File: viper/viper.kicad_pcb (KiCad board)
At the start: 2 copper layers, 127 parts, among them SW1 SW_Push, SW10 SW_Push, SW11 SW_Push, SW12 SW_Push, SW13 SW_Push, SW14 SW_Push, SW14_1 SW_Push, SW15 SW_Push, SW16 SW_Push, SW17 SW_Push, SW18 SW_Push, SW19 SW_Push, SW2 SW_Push, SW20 SW_Push, SW21 SW_Push, SW22 SW_Push, SW23 SW_Push, SW24 SW_Push, SW25 SW_Push, SW26 SW_Push, SW27 SW_Push, SW28 SW_Push, SW28_1 SW_Push, SW29 SW_Push, SW3 SW_Push, SW30 SW_Push, SW31 SW_Push, SW32 SW_Push, SW33 SW_Push, SW34 SW_Push, SW35 SW_Push, SW36 SW_Push, SW37 SW_Push, SW38 SW_Push, SW39 SW_Push, SW4 SW_Push, SW40 SW_Push, SW41 SW_Push, SW41_1 SW_Push, SW42 SW_Push, SW43 SW_Push, SW43_1 SW_Push, SW44 SW_Push, SW45 SW_Push, SW46 SW_Push, SW47 SW_Push, SW48 SW_Push, SW49 SW_Push, SW5 SW_Push, SW50 SW_Push, SW51 SW_Push, SW52 SW_Push, SW53 SW_Push, SW54 SW_Push, SW55 SW_Push, SW55_1 SW_Push, SW56 SW_Push, SW57 SW_Push, SW58 SW_Push, SW59 SW_Push, SW6 SW_Push, SW60 SW_Push, SW61 SW_Push, SW7 SW_Push, SW8 SW_Push, SW9 SW_Push

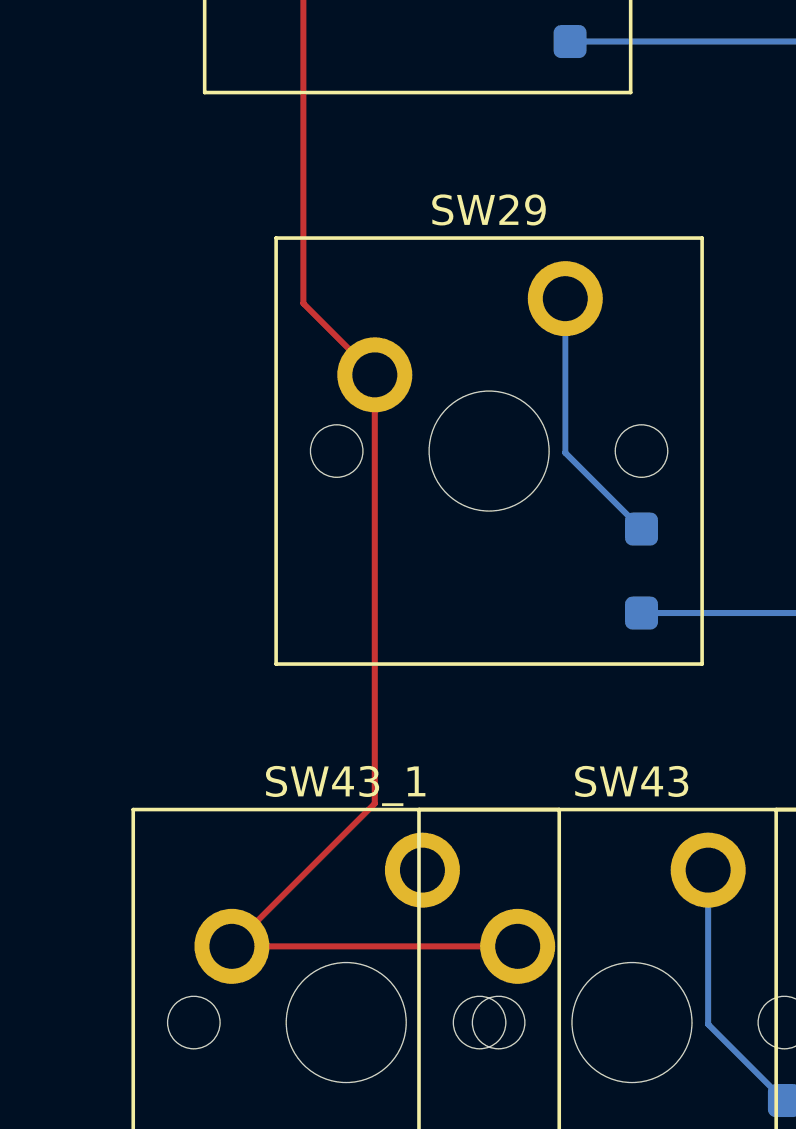
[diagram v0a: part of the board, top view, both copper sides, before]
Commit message: Add updated export with stepped caps
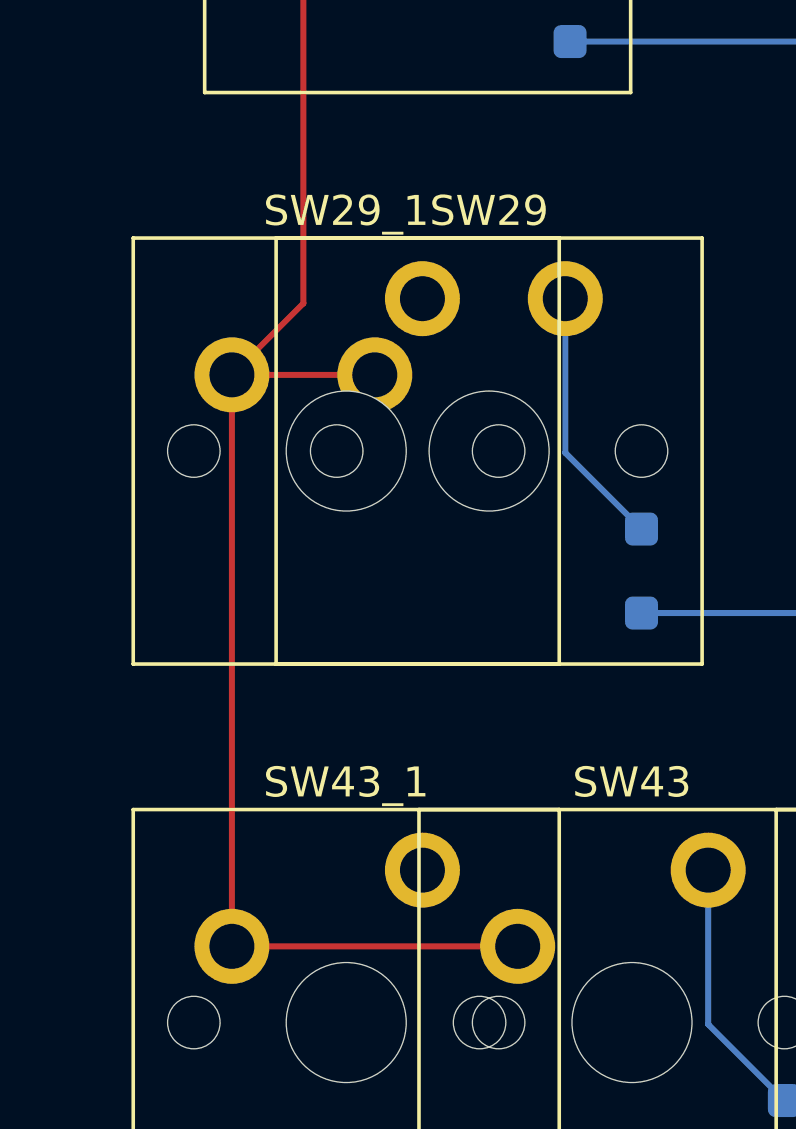
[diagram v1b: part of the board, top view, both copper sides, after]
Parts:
- added SW29_1: SW_Push, Switch_Keyboard_Cherry_MX:SW_Cherry_MX_PCB_1.00u, F.Cu at (97.6, 76.2)
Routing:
- net COL0: track 71.6 -> 74.4 mm

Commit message: kle2netlist with layout & netlist xml
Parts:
- removed SW14_1, SW28_1, SW29_1, SW41_1, SW43_1, SW55_1: SW_Push, Switch_Keyboard_Cherry_MX:SW_Cherry_MX_PCB_1.00u
- added C1: 22p, Capacitor_SMD:C_0603_1608Metric, B.Cu at (208.0, 161.7)
- added C2: 22p, Capacitor_SMD:C_0603_1608Metric, B.Cu at (207.6, 157.3)
- added C3: 0.1u, Capacitor_SMD:C_0603_1608Metric, B.Cu at (185.5, 164.3)
- added C4: 0.1u, Capacitor_SMD:C_0603_1608Metric, B.Cu at (195.3, 151.9)
- added C5: 0.1u, Capacitor_SMD:C_0603_1608Metric, B.Cu at (198.2, 169.4)
- added C6: 0.1u, Capacitor_SMD:C_0603_1608Metric, B.Cu at (185.5, 156.3)
- added C7: 4.7u, Capacitor_SMD:C_0603_1608Metric, B.Cu at (190.9, 151.9)
- added C8: 1u, Capacitor_SMD:C_0603_1608Metric, B.Cu at (195.3, 150.3)
- added D62: D, Diode_SMD:D_SOD-123F, B.Cu at (367.0, 98.3)
- added D63: D, Diode_SMD:D_SOD-123F, B.Cu at (128.9, 117.3)
- added D64: D, Diode_SMD:D_SOD-123F, B.Cu at (152.7, 117.3)
- added D65: D, Diode_SMD:D_SOD-123F, B.Cu at (233.7, 117.3)
- added D66: D, Diode_SMD:D_SOD-123F, B.Cu at (314.6, 117.3)
- added D67: D, Diode_SMD:D_SOD-123F, B.Cu at (338.5, 117.3)
- added J1: USB_C_Receptacle_USB2.0, Connector_USB:USB_C_Receptacle_XKB_U262-16XN-4BVC11, B.Cu at (192.7, 132.8)
- added R1: 22, Resistor_SMD:R_0603_1608Metric, B.Cu at (191.8, 147.8)
- added R2: 22, Resistor_SMD:R_0603_1608Metric, B.Cu at (193.5, 147.8)
- added R3: 10k, Resistor_SMD:R_0603_1608Metric, B.Cu at (190.9, 169.4)
- added R4: 10k, Resistor_SMD:R_0603_1608Metric, B.Cu at (206.0, 154.6)
- added RST: SW_SPST, Button_Switch_SMD:SW_SPST_TL3342, B.Cu at (215.7, 154.0)
- added ST14: MountingHole, PCM_Mounting_Keyboard_Stabilizer:Stabilizer_Cherry_MX_2.00u, F.Cu at (352.4, 38.1)
- added ST30: MountingHole, PCM_Mounting_Keyboard_Stabilizer:Stabilizer_Cherry_MX_2.00u, F.Cu at (359.6, 66.7)
- added ST44: MountingHole, PCM_Mounting_Keyboard_Stabilizer:Stabilizer_Cherry_MX_2.00u, F.Cu at (350.0, 76.2)
- added ST47: MountingHole, PCM_Mounting_Keyboard_Stabilizer:Stabilizer_Cherry_MX_2.00u, F.Cu at (107.2, 95.2)
- added ST60: MountingHole, PCM_Mounting_Keyboard_Stabilizer:Stabilizer_Cherry_MX_2.00u, F.Cu at (345.3, 95.2)
- added ST65: MountingHole, PCM_Mounting_Keyboard_Stabilizer:Stabilizer_Cherry_MX_7.00u, F.Cu at (228.6, 114.3)
- added SW62: SW_Push, PCM_Switch_Keyboard_Cherry_MX:SW_Cherry_MX_PCB_1.00u, F.Cu at (361.9, 95.2)
- added SW63: SW_Push, PCM_Switch_Keyboard_Cherry_MX:SW_Cherry_MX_PCB_1.00u, F.Cu at (123.8, 114.3)
- added SW64: SW_Push, PCM_Switch_Keyboard_Cherry_MX:SW_Cherry_MX_PCB_1.50u, F.Cu at (147.6, 114.3)
- added SW65: SW_Push, PCM_Switch_Keyboard_Cherry_MX:SW_Cherry_MX_PCB_7.00u, F.Cu at (228.6, 114.3)
- added SW66: SW_Push, PCM_Switch_Keyboard_Cherry_MX:SW_Cherry_MX_PCB_1.50u, F.Cu at (309.6, 114.3)
- added SW67: SW_Push, PCM_Switch_Keyboard_Cherry_MX:SW_Cherry_MX_PCB_1.00u, F.Cu at (333.4, 114.3)
- added U1: ATmega32U4-A, Package_QFP:TQFP-44_10x10mm_P0.8mm, B.Cu at (194.9, 160.3)
- added U2: TPD2S017, Package_TO_SOT_SMD:SOT-23-6, B.Cu at (192.7, 141.7)
- added Y1: Crystal_GND24, Crystal:Crystal_SMD_3225-4Pin_3.2x2.5mm, B.Cu at (205.6, 159.4)
- SW1, SW10, SW11, SW12, SW13, SW15, SW17, SW18, SW19, SW2, SW20, SW21, SW22, SW23, SW24, SW25, SW26, SW27, SW28, SW3, SW30, SW33, SW34, SW35, SW36, SW37, SW38, SW39, SW4, SW40, SW41, SW42, SW43, SW45, SW46, SW49, SW5, SW50, SW51, SW52, SW53, SW54, SW55, SW56, SW57, SW58, SW59, SW6, SW7, SW8, SW9: footprint Switch_Keyboard_Cherry_MX:SW_Cherry_MX_PCB_1.00u -> PCM_Switch_Keyboard_Cherry_MX:SW_Cherry_MX_PCB_1.00u
- SW14: footprint Switch_Keyboard_Cherry_MX:SW_Cherry_MX_PCB_1.00u -> PCM_Switch_Keyboard_Cherry_MX:SW_Cherry_MX_PCB_2.00u
- SW16, SW29: footprint Switch_Keyboard_Cherry_MX:SW_Cherry_MX_PCB_1.00u -> PCM_Switch_Keyboard_Cherry_MX:SW_Cherry_MX_PCB_1.50u
- SW31, SW61: footprint Switch_Keyboard_Cherry_MX:SW_Cherry_MX_PCB_1.00u -> PCM_Switch_Keyboard_Cherry_MX:SW_Cherry_MX_PCB_1.75u
- SW32, SW48: footprint Switch_Keyboard_Cherry_MX:SW_Cherry_MX_PCB_1.00u -> PCM_Switch_Keyboard_Cherry_MX:SW_Cherry_MX_PCB_1.25u
- SW44, SW47: footprint Switch_Keyboard_Cherry_MX:SW_Cherry_MX_PCB_1.00u -> PCM_Switch_Keyboard_Cherry_MX:SW_Cherry_MX_PCB_2.25u
- SW60: footprint Switch_Keyboard_Cherry_MX:SW_Cherry_MX_PCB_1.00u -> PCM_Switch_Keyboard_Cherry_MX:SW_Cherry_MX_PCB_2.75u
- moved D29 255.6 mm to (362.3, 60.2)
- moved SW29 255.5 mm to (357.2, 57.1)
- moved D15 243.7 mm to (348.0, 41.1)
- moved SW15 243.6 mm to (342.9, 38.1)
- moved D44 231.8 mm to (355.1, 79.2)
- moved SW44 231.8 mm to (350.0, 76.2)
- moved D30 231.2 mm to (364.6, 69.7)
- moved SW30 231.2 mm to (359.6, 66.7)
- moved D46 212.9 mm to (367.0, 41.1)
- moved D43 212.9 mm to (324.2, 79.2)
- moved SW43 212.8 mm to (319.1, 76.2)
- moved SW46 212.6 mm to (361.9, 38.1)
- moved D45 201.0 mm to (343.2, 79.2)
- moved SW45 200.9 mm to (338.1, 76.2)
- moved D57 149.0 mm to (276.5, 98.3)
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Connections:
- D15 pad 1: ROW1 -> ROW0
- D29 pad 1: ROW2 -> ROW1
- D30 pad 1: ROW2 -> ROW1
- D43 pad 1: ROW3 -> ROW2
- D44 pad 1: ROW3 -> ROW2
- D45 pad 1: ROW3 -> ROW2
- D46 pad 1: ROW3 -> ROW2
- D57 pad 1: ROW4 -> ROW3
- D58 pad 1: ROW4 -> ROW3
- D59 pad 1: ROW4 -> ROW3
- D60 pad 1: ROW4 -> ROW3
- D61 pad 1: ROW4 -> ROW3
- SW15 pad 1: COL0 -> COL13
- SW16 pad 1: COL1 -> COL0
- SW17 pad 1: COL2 -> COL1
- SW18 pad 1: COL3 -> COL2
- SW19 pad 1: COL4 -> COL3
- SW20 pad 1: COL5 -> COL4
- SW21 pad 1: COL6 -> COL5
- SW22 pad 1: COL7 -> COL6
- SW23 pad 1: COL8 -> COL7
- SW24 pad 1: COL9 -> COL8
- SW25 pad 1: COL10 -> COL9
- SW26 pad 1: COL11 -> COL10
- SW27 pad 1: COL12 -> COL11
- SW28 pad 1: COL13 -> COL12
- SW29 pad 1: COL0 -> COL13
- SW30 pad 1: COL1 -> COL13
- SW31 pad 1: COL2 -> COL0
- SW32 pad 1: COL3 -> COL0
- SW33 pad 1: COL4 -> COL1
- SW34 pad 1: COL5 -> COL2
- SW35 pad 1: COL6 -> COL3
- SW36 pad 1: COL7 -> COL4
- SW37 pad 1: COL8 -> COL5
- SW38 pad 1: COL9 -> COL6
- SW39 pad 1: COL10 -> COL7
- SW40 pad 1: COL11 -> COL8
- SW41 pad 1: COL12 -> COL9
- SW42 pad 1: COL13 -> COL10
- SW43 pad 1: COL0 -> COL11
- SW44 pad 1: COL1 -> COL12
- SW45 pad 1: COL2 -> COL12
- SW46 pad 1: COL3 -> COL13
- SW47 pad 1: COL4 -> COL0
- SW48 pad 1: COL5 -> COL0
- SW49 pad 1: COL6 -> COL1
- SW50 pad 1: COL7 -> COL2
- SW51 pad 1: COL8 -> COL3
- SW52 pad 1: COL9 -> COL4
- SW53 pad 1: COL10 -> COL5
- SW54 pad 1: COL11 -> COL6
- SW55 pad 1: COL12 -> COL7
- SW56 pad 1: COL13 -> COL8
- SW57 pad 1: COL1 -> COL9
- SW58 pad 1: COL2 -> COL10
- SW59 pad 1: COL3 -> COL11
- SW60 pad 1: COL11 -> COL12
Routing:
- net ROW3: track 254.8 -> 528.6 mm
- net ROW0: track 257.2 -> 514.3 mm
- net ROW1: track 233.4 -> 466.7 mm
- net ROW2: track 290.7 -> 504.8 mm
- net COL2: track 90.0 -> 270.0 mm
- net COL11: track 86.1 -> 258.2 mm
- net COL9: track 67.0 -> 201.0 mm
- net COL4: track 67.0 -> 201.0 mm
- net COL8: track 67.0 -> 201.0 mm
- net COL6: track 67.0 -> 201.0 mm
- net COL5: track 67.0 -> 201.0 mm
- net COL7: track 67.0 -> 201.0 mm
- net ROW4: track 209.5 -> 338.1 mm
- net COL0: track 74.4 -> 199.4 mm
- net COL10: track 44.0 -> 132.1 mm
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
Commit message: Updated kle layout
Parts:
- removed D62, D63, D64, D65, D66, D67: D, Diode_SMD:D_SOD-123F
- removed ST30, ST44, ST47, ST60: MountingHole, PCM_Mounting_Keyboard_Stabilizer:Stabilizer_Cherry_MX_2.00u
- removed ST65: MountingHole, PCM_Mounting_Keyboard_Stabilizer:Stabilizer_Cherry_MX_7.00u
- removed SW63, SW67: SW_Push, PCM_Switch_Keyboard_Cherry_MX:SW_Cherry_MX_PCB_1.00u
- removed SW64, SW66: SW_Push, PCM_Switch_Keyboard_Cherry_MX:SW_Cherry_MX_PCB_1.50u
- removed SW65: SW_Push, PCM_Switch_Keyboard_Cherry_MX:SW_Cherry_MX_PCB_7.00u
- added ST28_1: MountingHole, PCM_Mounting_Keyboard_Stabilizer:Stabilizer_Cherry_MX_2.00u, F.Cu at (111.9, 24.8)
- added ST41: MountingHole, PCM_Mounting_Keyboard_Stabilizer:Stabilizer_Cherry_MX_2.00u, F.Cu at (81.0, 24.8)
- added ST43: MountingHole, PCM_Mounting_Keyboard_Stabilizer:Stabilizer_Cherry_MX_2.00u, F.Cu at (142.7, 24.8)
- added ST55: MountingHole, PCM_Mounting_Keyboard_Stabilizer:Stabilizer_Cherry_MX_2.00u, F.Cu at (173.6, 24.8)
- added ST59: MountingHole, PCM_Mounting_Keyboard_Stabilizer:Stabilizer_Cherry_MX_7.00u, F.Cu at (95.3, 46.6)
- added SW14_1: SW_Push, PCM_Switch_Keyboard_Cherry_MX:SW_Cherry_MX_PCB_1.00u, F.Cu at (131.2, 172.3)
- added SW28_1: SW_Push, PCM_Switch_Keyboard_Cherry_MX:SW_Cherry_MX_PCB_1.00u, F.Cu at (113.7, 67.0)
- added SW29_1: SW_Push, PCM_Switch_Keyboard_Cherry_MX:SW_Cherry_MX_PCB_1.25u, F.Cu at (131.2, 137.2)
- added SW41_1: SW_Push, PCM_Switch_Keyboard_Cherry_MX:SW_Cherry_MX_PCB_1.00u, F.Cu at (148.8, 102.1)
- added SW43_1: SW_Push, PCM_Switch_Keyboard_Cherry_MX:SW_Cherry_MX_PCB_1.25u, F.Cu at (113.7, 84.6)
- added SW55_1: SW_Push, PCM_Switch_Keyboard_Cherry_MX:SW_Cherry_MX_PCB_1.75u, F.Cu at (183.9, 102.1)
- C1, C2, C3, C4, C5, C6, C7, C8, D1, D10, D11, D12, D13, D14, D15, D16, D17, D18, D19, D2, D20, D21, D22, D23, D24, D25, D26, D27, D28, D29, D3, D30, D31, D32, D33, D34, D35, D36, D37, D38, D39, D4, D40, D41, D42, D43, D44, D45, D46, D47, D48, D49, D5, D50, D51, D52, D53, D54, D55, D56, D57, D58, D59, D6, D60, D61, D7, D8, D9, R1, R2, R3, R4, RST, U2, Y1: moved to F.Cu
- J1: value USB_C_Receptacle_USB2.0 -> USB_C_Receptacle_USB2.0_14P; footprint Connector_USB:USB_C_Receptacle_XKB_U262-16XN-4BVC11 -> Connector_USB:USB_C_Receptacle_GCT_USB4105-xx-A_16P_TopMnt_Horizontal; moved to F.Cu
- SW15, SW28, SW58: footprint PCM_Switch_Keyboard_Cherry_MX:SW_Cherry_MX_PCB_1.00u -> PCM_Switch_Keyboard_Cherry_MX:SW_Cherry_MX_PCB_1.50u
- SW16: footprint PCM_Switch_Keyboard_Cherry_MX:SW_Cherry_MX_PCB_1.50u -> PCM_Switch_Keyboard_Cherry_MX:SW_Cherry_MX_PCB_1.00u
- SW29: footprint PCM_Switch_Keyboard_Cherry_MX:SW_Cherry_MX_PCB_1.50u -> PCM_Switch_Keyboard_Cherry_MX:SW_Cherry_MX_PCB_1.75u
- SW31, SW61: footprint PCM_Switch_Keyboard_Cherry_MX:SW_Cherry_MX_PCB_1.75u -> PCM_Switch_Keyboard_Cherry_MX:SW_Cherry_MX_PCB_1.00u
- SW32, SW48: footprint PCM_Switch_Keyboard_Cherry_MX:SW_Cherry_MX_PCB_1.25u -> PCM_Switch_Keyboard_Cherry_MX:SW_Cherry_MX_PCB_1.00u
- SW41, SW43: footprint PCM_Switch_Keyboard_Cherry_MX:SW_Cherry_MX_PCB_1.00u -> PCM_Switch_Keyboard_Cherry_MX:SW_Cherry_MX_PCB_2.25u
- SW44, SW47: footprint PCM_Switch_Keyboard_Cherry_MX:SW_Cherry_MX_PCB_2.25u -> PCM_Switch_Keyboard_Cherry_MX:SW_Cherry_MX_PCB_1.00u
- SW55: footprint PCM_Switch_Keyboard_Cherry_MX:SW_Cherry_MX_PCB_1.00u -> PCM_Switch_Keyboard_Cherry_MX:SW_Cherry_MX_PCB_2.75u
- SW59: footprint PCM_Switch_Keyboard_Cherry_MX:SW_Cherry_MX_PCB_1.00u -> PCM_Switch_Keyboard_Cherry_MX:SW_Cherry_MX_PCB_7.00u
- SW60: footprint PCM_Switch_Keyboard_Cherry_MX:SW_Cherry_MX_PCB_2.75u -> PCM_Switch_Keyboard_Cherry_MX:SW_Cherry_MX_PCB_1.50u
- SW62: value SW_Push -> SW_PUSH; footprint PCM_Switch_Keyboard_Cherry_MX:SW_Cherry_MX_PCB_1.00u -> Button_Switch_SMD:SW_SPST_TL3342
- U1: value ATmega32U4-A -> ATmega32U4-M; footprint Package_QFP:TQFP-44_10x10mm_P0.8mm -> Package_DFN_QFN:QFN-44-1EP_7x7mm_P0.5mm_EP5.2x5.2mm; moved to F.Cu
- moved SW62 369.4 mm to (4.28, 3.02)
- moved SW29 313.9 mm to (43.5, 67.0)
- moved SW46 304.5 mm to (61.0, 84.6)
- moved ST14 302.6 mm to (50.1, 24.8)
- moved D11 301.3 mm to (63.5, 183.8), turned to 0 degrees
- moved SW14 285.7 mm to (78.6, 119.7)
- moved SW12 270.3 mm to (61.0, 154.8)
- moved SW13 261.8 mm to (43.5, 137.2)
- moved SW45 260.9 mm to (78.6, 102.1)
- moved SW61 260.6 mm to (78.6, 137.2)
- moved SW43 259.0 mm to (78.6, 172.3)
- moved D24 255.7 mm to (38.5, 183.8), turned to 0 degrees
- moved D58 254.4 mm to (56.0, 183.8), turned to 0 degrees
- moved D60 249.3 mm to (116.2, 183.8), turned to 0 degrees
- moved SW15 248.5 mm to (96.1, 67.0)
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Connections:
- net N$1 renamed /N$1
- net N$10 renamed /N$10
- net N$11 renamed /N$11
- net N$12 renamed /N$12
- net N$13 renamed /N$13
- net N$14 renamed /N$14
- net N$15 renamed /N$15
- net N$16 renamed /N$16
- net N$17 renamed /N$17
- net N$18 renamed /N$18
- net N$19 renamed /N$19
- net N$2 renamed /N$2
- net N$20 renamed /N$20
- net N$21 renamed /N$21
- net N$22 renamed /N$22
- net N$23 renamed /N$23
- net N$24 renamed /N$24
- net N$25 renamed /N$25
- net N$26 renamed /N$26
- net N$27 renamed /N$27
- net N$28 renamed /N$28
- net N$29 renamed /N$29
- net N$3 renamed /N$3
- net N$30 renamed /N$30
- net N$31 renamed /N$31
- net N$32 renamed /N$32
- net N$33 renamed /N$33
- net N$34 renamed /N$34
- net N$35 renamed /N$35
- net N$36 renamed /N$36
- net N$37 renamed /N$37
- net N$38 renamed /N$38
- net N$39 renamed /N$39
- net N$4 renamed /N$4
- net N$40 renamed /N$40
- net N$41 renamed /N$41
- net N$42 renamed /N$42
- net N$43 renamed /N$43
- net N$44 renamed /N$44
- net N$45 renamed /N$45
- net N$46 renamed /N$46
- net N$47 renamed /N$47
- net N$48 renamed /N$48
- net N$49 renamed /N$49
- net N$5 renamed /N$5
- net N$50 renamed /N$50
- net N$51 renamed /N$51
- net N$52 renamed /N$52
- net N$53 renamed /N$53
- net N$54 renamed /N$54
- net N$55 renamed /N$55
- net N$56 renamed /N$56
- net N$57 renamed /N$57
- net N$58 renamed /N$58
- net N$59 renamed /N$59
- net N$6 renamed /N$6
- net N$60 renamed /N$60
- net N$61 renamed /N$61
- net N$7 renamed /N$7
- net N$8 renamed /N$8
- net N$9 renamed /N$9
- C1 pad 1: mcu/XTAL1 -> /UCAP
- C2 pad 1: mcu/XTAL2 -> GND
- C2 pad 2: GND -> VCC
- C3 pad 1: VCC -> GND
- C3 pad 2: GND -> VCC
- C4 pad 1: VCC -> GND
- C4 pad 2: GND -> VCC
- C5 pad 1: VCC -> GND
- C5 pad 2: GND -> VCC
- C6 pad 1: VCC -> GND
- C6 pad 2: GND -> VCC
- D15 pad 1: ROW0 -> ROW1
- D29 pad 1: ROW1 -> ROW2
- D30 pad 1: ROW1 -> ROW2
- D43 pad 1: ROW2 -> ROW3
- D44 pad 1: ROW2 -> ROW3
- D45 pad 1: ROW2 -> ROW3
- D46 pad 1: ROW2 -> ROW3
- D57 pad 1: ROW3 -> ROW4
- D58 pad 1: ROW3 -> ROW4
- D59 pad 1: ROW3 -> ROW4
- D60 pad 1: ROW3 -> ROW4
- D61 pad 1: ROW3 -> ROW4
- J1 pad A1: GND -> (no net)
- J1 pad A12: GND -> (no net)
- J1 pad A4: VCC -> (no net)
- J1 pad A6: usb/D+ -> (no net)
- J1 pad A7: usb/D- -> (no net)
- J1 pad A9: VCC -> (no net)
- J1 pad B1: GND -> (no net)
- J1 pad B12: GND -> (no net)
- J1 pad B4: VCC -> (no net)
- J1 pad B6: usb/D+ -> (no net)
- J1 pad B7: usb/D- -> (no net)
- J1 pad B9: VCC -> (no net)
- J1 pad S1: GND -> (no net)
- R1 pad 1: mcu/D- -> D+
- R1 pad 2: u2/D- -> D+
- R2 pad 1: mcu/D+ -> D+
- R2 pad 2: u2/D+ -> D+
- R3 pad 1: mcu/~{HWB}/PE2 -> GND
- R4 pad 1: mcu/~{RESET} -> ~{RESET}
- R4 pad 2: VCC -> GND
- SW15 pad 1: COL13 -> COL0
- SW16 pad 1: COL0 -> COL1
- SW17 pad 1: COL1 -> COL2
- SW18 pad 1: COL2 -> COL3
- SW19 pad 1: COL3 -> COL4
- SW20 pad 1: COL4 -> COL5
- SW21 pad 1: COL5 -> COL6
- SW22 pad 1: COL6 -> COL7
- SW23 pad 1: COL7 -> COL8
- SW24 pad 1: COL8 -> COL9
- SW25 pad 1: COL9 -> COL10
- SW26 pad 1: COL10 -> COL11
- SW27 pad 1: COL11 -> COL12
- SW28 pad 1: COL12 -> COL13
- SW29 pad 1: COL13 -> COL0
- SW30 pad 1: COL13 -> COL1
- SW31 pad 1: COL0 -> COL2
- SW32 pad 1: COL0 -> COL3
- SW33 pad 1: COL1 -> COL4
- SW34 pad 1: COL2 -> COL5
- SW35 pad 1: COL3 -> COL6
- SW36 pad 1: COL4 -> COL7
- SW37 pad 1: COL5 -> COL8
- SW38 pad 1: COL6 -> COL9
- SW39 pad 1: COL7 -> COL10
- SW40 pad 1: COL8 -> COL11
- SW41 pad 1: COL9 -> COL12
- SW42 pad 1: COL10 -> COL13
- SW43 pad 1: COL11 -> COL0
- SW44 pad 1: COL12 -> COL1
- SW45 pad 1: COL12 -> COL2
- SW46 pad 1: COL13 -> COL3
- SW47 pad 1: COL0 -> COL4
- SW48 pad 1: COL0 -> COL5
- SW49 pad 1: COL1 -> COL6
- SW50 pad 1: COL2 -> COL7
- SW51 pad 1: COL3 -> COL8
- SW52 pad 1: COL4 -> COL9
- SW53 pad 1: COL5 -> COL10
- SW54 pad 1: COL6 -> COL11
- SW55 pad 1: COL7 -> COL12
- SW56 pad 1: COL8 -> COL13
- SW57 pad 1: COL9 -> COL1
- SW58 pad 1: COL10 -> COL2
- SW59 pad 1: COL11 -> COL3
- SW60 pad 1: COL12 -> COL11
- SW62 pad 1: COL13 -> GND
- SW62 pad 2: N$62 -> RST
- U1 pad 1: (no net) -> row4
- U1 pad 12: COL2 -> COL10
- U1 pad 13: mcu/~{RESET} -> ~{RESET}
- U1 pad 16: mcu/XTAL2 -> /XTAL2
- U1 pad 17: mcu/XTAL1 -> /UCAP
- U1 pad 18: COL5 -> COL13
- U1 pad 19: COL6 -> COL2
- U1 pad 20: COL7 -> COL3
- U1 pad 21: COL8 -> COL4
- U1 pad 22: COL10 -> COL6
- U1 pad 25: COL9 -> COL5
- U1 pad 26: COL11 -> COL7
- U1 pad 27: COL12 -> COL8
- U1 pad 3: mcu/D- -> D+
- U1 pad 31: COL3 -> COL11
- U1 pad 32: COL4 -> COL12
- U1 pad 33: mcu/~{HWB}/PE2 -> /PE2
- U1 pad 36: (no net) -> col14
- U1 pad 37: (no net) -> col13
- U1 pad 38: (no net) -> col12
- U1 pad 39: (no net) -> col11
- U1 pad 4: mcu/D+ -> D+
- U1 pad 40: (no net) -> col10
- U1 pad 41: COL13 -> COL9
- U1 pad 42: (no net) -> unconnected-(U1-AREF-Pad42)
- U1 pad 6: mcu/UCAP -> /UCAP
- U2 pad 1: u2/D- -> D+
- U2 pad 3: usb/D- -> D+
- U2 pad 4: usb/D+ -> D+
- U2 pad 5: VCC -> VBUS
- U2 pad 6: u2/D+ -> D+
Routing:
- net ROW3: track 528.6 -> 0.00 mm
- net ROW0: track 514.3 -> 0.00 mm
- net ROW2: track 504.8 -> 0.00 mm
- net ROW1: track 466.7 -> 0.00 mm
- net ROW4: track 338.1 -> 0.00 mm
- net COL2: track 270.0 -> 0.00 mm
- net COL11: track 258.2 -> 0.00 mm
- net COL9: track 201.0 -> 0.00 mm
- net COL4: track 201.0 -> 0.00 mm
- net COL6: track 201.0 -> 0.00 mm
- net COL8: track 201.0 -> 0.00 mm
- net COL5: track 201.0 -> 0.00 mm
- net COL7: track 201.0 -> 0.00 mm
- net COL0: track 199.4 -> 0.00 mm
- net COL12: track 166.6 -> 0.00 mm
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
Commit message: MX Hybrid PCB, diode alignment is strange
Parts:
- removed C1, C2: 22p, Capacitor_SMD:C_0603_1608Metric
- removed C3, C4, C5, C6: 0.1u, Capacitor_SMD:C_0603_1608Metric
- removed C7: 4.7u, Capacitor_SMD:C_0603_1608Metric
- removed C8: 1u, Capacitor_SMD:C_0603_1608Metric
- removed J1: USB_C_Receptacle_USB2.0_14P, Connector_USB:USB_C_Receptacle_GCT_USB4105-xx-A_16P_TopMnt_Horizontal
- removed R1, R2: 22, Resistor_SMD:R_0603_1608Metric
- removed R3, R4: 10k, Resistor_SMD:R_0603_1608Metric
- removed RST: SW_SPST, Button_Switch_SMD:SW_SPST_TL3342
- removed ST14, ST28_1, ST41, ST43, ST55: MountingHole, PCM_Mounting_Keyboard_Stabilizer:Stabilizer_Cherry_MX_2.00u
- removed ST59: MountingHole, PCM_Mounting_Keyboard_Stabilizer:Stabilizer_Cherry_MX_7.00u
- removed SW62: SW_PUSH, Button_Switch_SMD:SW_SPST_TL3342
- removed U1: ATmega32U4-M, Package_DFN_QFN:QFN-44-1EP_7x7mm_P0.5mm_EP5.2x5.2mm
- removed U2: TPD2S017, Package_TO_SOT_SMD:SOT-23-6
- removed Y1: Crystal_GND24, Crystal:Crystal_SMD_3225-4Pin_3.2x2.5mm
- SW1, SW10, SW11, SW12, SW13, SW14_1, SW16, SW17, SW18, SW19, SW2, SW20, SW21, SW22, SW23, SW24, SW25, SW26, SW27, SW28_1, SW3, SW30, SW31, SW32, SW33, SW34, SW35, SW36, SW37, SW38, SW39, SW4, SW40, SW41_1, SW42, SW44, SW45, SW46, SW47, SW48, SW49, SW5, SW50, SW51, SW52, SW53, SW54, SW56, SW57, SW6, SW61, SW7, SW8, SW9: footprint PCM_Switch_Keyboard_Cherry_MX:SW_Cherry_MX_PCB_1.00u -> Switch_Keyboard_Hybrid:SW_Hybrid_Cherry_MX_Alps_1.00u
- SW14: footprint PCM_Switch_Keyboard_Cherry_MX:SW_Cherry_MX_PCB_2.00u -> Switch_Keyboard_Hybrid:SW_Hybrid_Cherry_MX_Alps_1.00u
- SW15, SW28, SW58, SW60: footprint PCM_Switch_Keyboard_Cherry_MX:SW_Cherry_MX_PCB_1.50u -> Switch_Keyboard_Hybrid:SW_Hybrid_Cherry_MX_Alps_1.00u
- SW29, SW55_1: footprint PCM_Switch_Keyboard_Cherry_MX:SW_Cherry_MX_PCB_1.75u -> Switch_Keyboard_Hybrid:SW_Hybrid_Cherry_MX_Alps_1.00u
- SW29_1, SW43_1: footprint PCM_Switch_Keyboard_Cherry_MX:SW_Cherry_MX_PCB_1.25u -> Switch_Keyboard_Hybrid:SW_Hybrid_Cherry_MX_Alps_1.00u
- SW41, SW43: footprint PCM_Switch_Keyboard_Cherry_MX:SW_Cherry_MX_PCB_2.25u -> Switch_Keyboard_Hybrid:SW_Hybrid_Cherry_MX_Alps_1.00u
- SW55: footprint PCM_Switch_Keyboard_Cherry_MX:SW_Cherry_MX_PCB_2.75u -> Switch_Keyboard_Hybrid:SW_Hybrid_Cherry_MX_Alps_1.00u
- SW59: footprint PCM_Switch_Keyboard_Cherry_MX:SW_Cherry_MX_PCB_7.00u -> Switch_Keyboard_Hybrid:SW_Hybrid_Cherry_MX_Alps_1.00u
- moved D24 359.3 mm to (125.0, -165.0)
- moved D20 358.8 mm to (114.6, -165.0)
- moved D15 357.7 mm to (99.0, -158.6)
- moved D14 357.7 mm to (99.0, -165.0)
- moved D36 355.7 mm to (156.1, -165.0)
- moved D12 354.9 mm to (93.8, -165.0)
- moved D59 353.4 mm to (62.6, -152.2)
- moved D6 353.2 mm to (78.2, -165.0)
- moved D17 353.1 mm to (104.2, -158.6)
- moved D9 352.7 mm to (83.4, -158.6)
- moved D26 352.1 mm to (130.2, -165.0)
- moved D18 350.6 mm to (109.4, -165.0)
- moved D31 350.6 mm to (140.6, -158.6)
- moved D16 349.0 mm to (104.2, -165.0)
- moved D37 348.5 mm to (156.1, -158.6)
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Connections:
- net /N$1 renamed Net-(D1-A)
- net /N$10 renamed Net-(D10-A)
- net /N$11 renamed Net-(D11-A)
- net /N$12 renamed Net-(D12-A)
- net /N$13 renamed Net-(D13-A)
- net /N$14 renamed Net-(D14-A)
- net /N$15 renamed Net-(D15-A)
- net /N$16 renamed Net-(D16-A)
- net /N$17 renamed Net-(D17-A)
- net /N$18 renamed Net-(D18-A)
- net /N$19 renamed Net-(D19-A)
- net /N$2 renamed Net-(D2-A)
- net /N$20 renamed Net-(D20-A)
- net /N$21 renamed Net-(D21-A)
- net /N$22 renamed Net-(D22-A)
- net /N$23 renamed Net-(D23-A)
- net /N$24 renamed Net-(D24-A)
- net /N$25 renamed Net-(D25-A)
- net /N$26 renamed Net-(D26-A)
- net /N$27 renamed Net-(D27-A)
- net /N$28 renamed Net-(D28-A)
- net /N$29 renamed Net-(D29-A)
- net /N$3 renamed Net-(D3-A)
- net /N$30 renamed Net-(D30-A)
- net /N$31 renamed Net-(D31-A)
- net /N$32 renamed Net-(D32-A)
- net /N$33 renamed Net-(D33-A)
- net /N$34 renamed Net-(D34-A)
- net /N$35 renamed Net-(D35-A)
- net /N$36 renamed Net-(D36-A)
- net /N$37 renamed Net-(D37-A)
- net /N$38 renamed Net-(D38-A)
- net /N$39 renamed Net-(D39-A)
- net /N$4 renamed Net-(D4-A)
- net /N$40 renamed Net-(D40-A)
- net /N$41 renamed Net-(D41-A)
- net /N$42 renamed Net-(D42-A)
- net /N$43 renamed Net-(D43-A)
- net /N$44 renamed Net-(D44-A)
- net /N$45 renamed Net-(D45-A)
- net /N$46 renamed Net-(D46-A)
- net /N$47 renamed Net-(D47-A)
- net /N$48 renamed Net-(D48-A)
- net /N$49 renamed Net-(D49-A)
- net /N$5 renamed Net-(D5-A)
- net /N$50 renamed Net-(D50-A)
- net /N$51 renamed Net-(D51-A)
- net /N$52 renamed Net-(D52-A)
- net /N$53 renamed Net-(D53-A)
- net /N$54 renamed Net-(D54-A)
- net /N$55 renamed Net-(D55-A)
- net /N$56 renamed Net-(D56-A)
- net /N$57 renamed Net-(D57-A)
- net /N$58 renamed Net-(D58-A)
- net /N$59 renamed Net-(D59-A)
- net /N$6 renamed Net-(D6-A)
- net /N$60 renamed Net-(D60-A)
- net /N$61 renamed Net-(D61-A)
- net /N$7 renamed Net-(D7-A)
- net /N$8 renamed Net-(D8-A)
- net /N$9 renamed Net-(D9-A)
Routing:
- net COL12: track 0.00 -> 98.3 mm
- net COL1: track 0.00 -> 83.3 mm
- net COL0: track 0.00 -> 69.1 mm
- net COL9: track 0.00 -> 63.2 mm
- net COL10: track 0.00 -> 63.2 mm
- net COL4: track 0.00 -> 63.2 mm
- net COL8: track 0.00 -> 63.2 mm
- net COL6: track 0.00 -> 63.2 mm
- net COL5: track 0.00 -> 63.2 mm
- net COL7: track 0.00 -> 63.2 mm
- net COL11: track 0.00 -> 60.3 mm
- net COL2: track 0.00 -> 44.2 mm
- net COL3: track 0.00 -> 43.1 mm
- net COL13: track 0.00 -> 27.2 mm
- net ROW2: track 0.00 -> 12.8 mm
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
